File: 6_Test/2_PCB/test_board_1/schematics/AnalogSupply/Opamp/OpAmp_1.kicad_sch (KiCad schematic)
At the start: 3 parts, among them U1 ADA4807-1AKSZ-R7

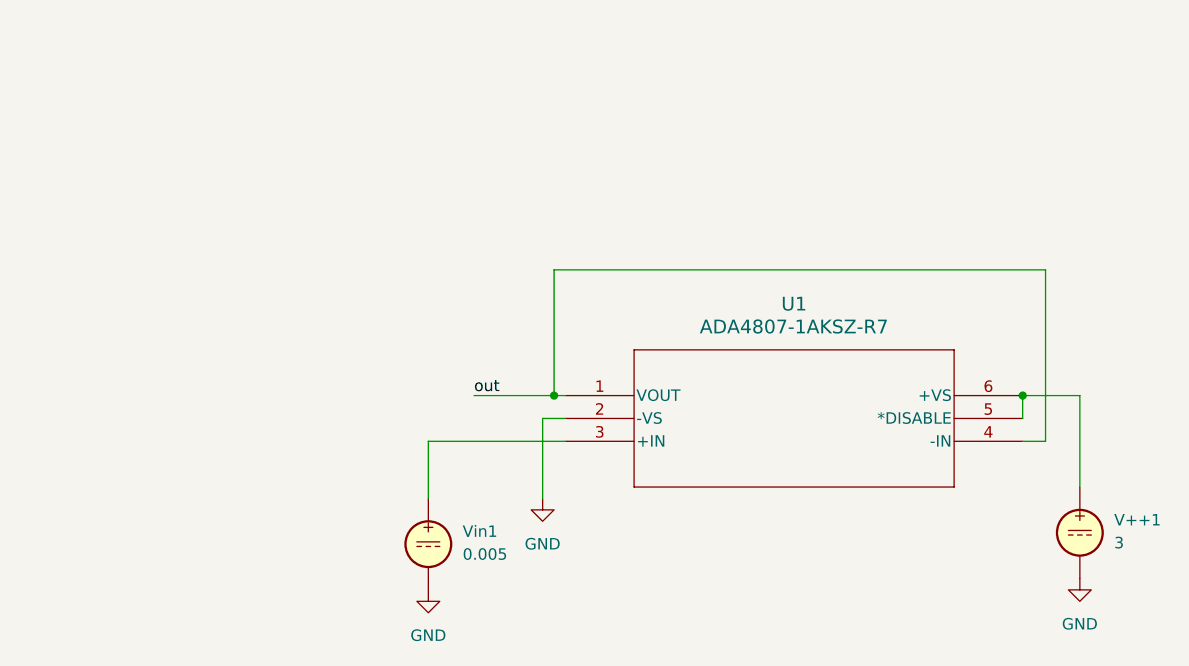
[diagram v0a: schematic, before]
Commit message: op amps done simulating
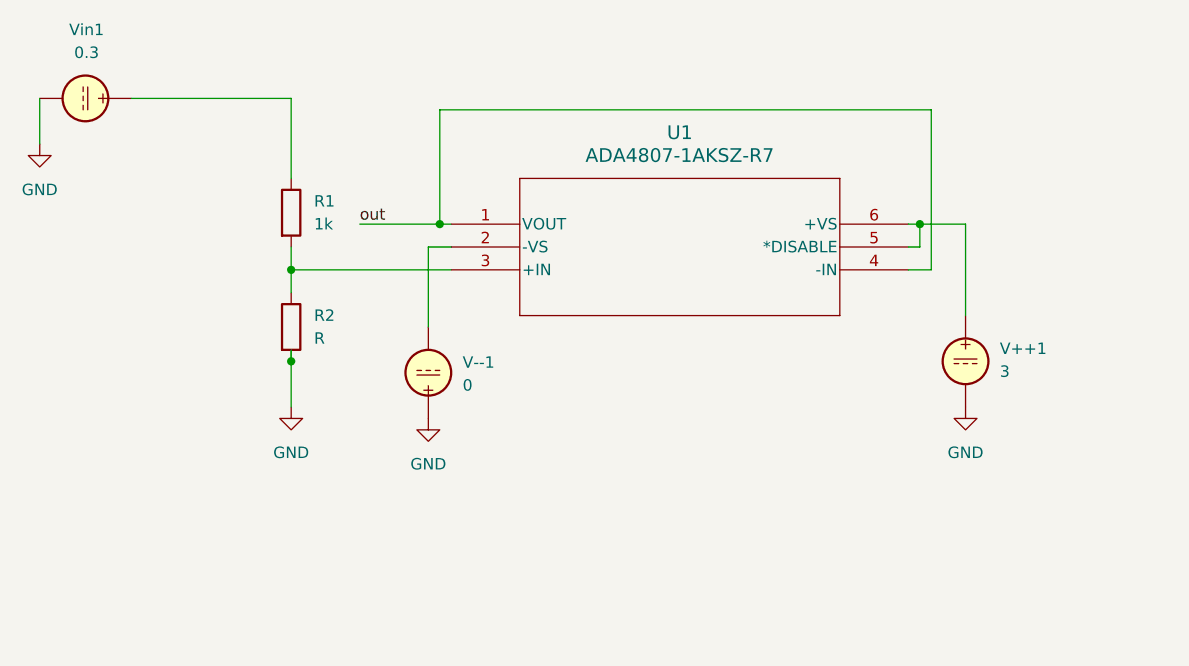
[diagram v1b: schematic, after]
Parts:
- added R1: 1k, symbol Device:R
- added R2: R, symbol Device:R
- added V--1: 0, symbol Simulation_SPICE:VDC
- Vin1: value 0.005 -> 0.3
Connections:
- net GND: now also R2.2, V--1.1; no longer U1.2 (-VS)
- net at U1.3 (+IN): now also R1.2, R2.1; no longer Vin1.1
- new net: R1.1, Vin1.1
- new net: U1.2 (-VS), V--1.2
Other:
- moved on the sheet: U1, V++1, Vin1
